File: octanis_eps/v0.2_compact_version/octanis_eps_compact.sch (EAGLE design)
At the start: 152 parts, among them IC10 OPA2333DGK, IC11 OPA2333DGK, IC12 OPA2333DGK, IC2 OPA2333DGK, IC3 OPA2333DGK, IC4 OPA2333DGK, IC5 OPA2333DGK, IC6 OPA2333DGK, IC7 OPA2333DGK, IC8 OPA2333DGK, IC9 OPA2333DGK, Q1 FC-12M

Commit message: modified compact version schematics
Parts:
- removed C1: 10nF, rcl:C-EUC0603
- removed C12: 1uF, rcl:CPOL-EUA/3216-18R
- removed C13: 470pF, rcl:C-EUC0603
- removed C16: 1n, rcl:C-EUC0603
- removed C17: 1u, rcl:CPOL-EUA/3216-18R
- removed C18: 1u, rcl:C-EUC0603
- removed C19: 22u, rcl:CPOL-EUA/3216-18R
- removed C_IC10, C_IC11, C_IC12, C_IC2, C_IC4, C_IC8: 100nF, rcl:C-EUC0603
- removed DISSIP1, DISSIP2: MP725TO-252, Octanis1_EPS:MP725TO-252
- removed IC10, IC11, IC12, IC2, IC4, IC8: OPA2333DGK, linear:OPA2333DGK
- removed L1: 4.7uH, inductors:DR73
- removed L2: 0.47uH, inductors:DR73
- removed LTC3411: LT3411, Octanis1_EPS:LT3411
- removed R30, R31, R4: 162k, rcl:R-EU_R0603
- removed R33, R38, R46, R47, R49, R50, R65: 100k, rcl:R-EU_R0603
- removed R34: 13k7, rcl:R-EU_R0603
- removed R35: 29k4, rcl:R-EU_R0603
- removed R36, R44: 19k6, rcl:R-EU_R0603
- removed R37: 27k4, rcl:R-EU_R0603
- removed R39, R57: 50m, rcl:R-EU_R1206
- removed R40, R41, R63, R71: 22k1, rcl:R-EU_R0603
- removed R42, R5: 75k, rcl:R-EU_R0603
- removed R43, R45, R58, R62: 270k, rcl:R-EU_R0603
- removed R51, R52, R53: 200k, rcl:R-EU_R0603
- removed R54, R61, R64, R70: 1M, rcl:R-EU_R0603
- removed R55: 140k, rcl:R-EU_R0603
- removed R56: 43k2, rcl:R-EU_R0603
- removed R59: 330k, rcl:R-EU_R0603
- removed R60: 24k9, rcl:R-EU_R0603
- removed SC_BOT: (no value), jumper:JP4E
- added 0.47UH, 10UH: DR127, inductors:DR127
- added HEAT1, HEAT2, HEAT3, HEAT_SINK: (no value), jumper:JP1E
- added U$10, U$9: MBRM120LTIG, Octanis1_EPS:MBRM120LTIG
- added U$12, U$20, U$21: IRFR3711ZTRPBF, Octanis1_EPS:IRFR3711ZTRPBF
- C10: value 100nF -> 22u
- C11: value 100nF -> 4.7p
- C4: value 150nF -> 4.7u
- C5: value 150nF -> 470p
- C8: value 1nF -> 22u
- C9: value 22uF -> 10u; device rcl:CPOL-EUA/3216-18R -> rcl:C-EUC0603
- R1: value 33k -> 1k
- R10: value 50m -> 30.1k; device rcl:R-EU_R1206 -> rcl:R-EU_R0603
- R11: value 10k -> 549k
- R12: value 50m -> 1.3M; device rcl:R-EU_R1206 -> rcl:R-EU_R0603
- R13: value 10k -> 1M
- R2: value 20k -> 1k
- R3: value 1M -> 1k
- R32: value 162k -> 82k
- U$11: value LTC3421 -> MBRM120LTIG; device Octanis1_EPS:LTC3421 -> Octanis1_EPS:MBRM120LTIG
- U$2, U$3: value MAX4376FASASO8 -> INA213; device Octanis1_EPS:MAX4376FASASO8 -> Octanis1_EPS:INA213
- U$4: value MAX4376FASASO8 -> LTC3402; device Octanis1_EPS:MAX4376FASASO8 -> Octanis1_EPS:LTC3402
- U$5: value MAX4376FASASO8 -> TPS62086; device Octanis1_EPS:MAX4376FASASO8 -> Octanis1_EPS:TPS62086
- U$8: value FDV301N -> MBRM120LTIG; device Octanis1_EPS:FDV301N -> Octanis1_EPS:MBRM120LTIG
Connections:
- removed net BT_IN: BT_IN.3, BT_IN.4, R10.1, R12.2, U$4.RS+, U$5.RS-
- removed net CHG_CMD: C1.2, IC2B.OUT, R31.2, R49.2
- removed net I_CHG_MS: IC4A.-IN, IC4A.OUT, U$1.7
- removed net I_DSG_MS: IC4B.-IN, IC4B.OUT, U$1.8
- removed net N$32: R37.1, U$11.RT
- removed net N$33: C11.2, U$11.SS
- removed net N$35: C18.2, R60.2
- removed net N$36: R38.1, U$11.VC
- removed net N$38: IC10B.+IN, R40.2, R45.2
- removed net N$39: IC10B.-IN, R41.2, R43.1
- removed net N$40: R9.2, U$2.OUT
- removed net N$41: R11.2, U$4.OUT
- removed net N$42: R7.2, U$3.OUT
- removed net N$43: R13.2, U$5.OUT
- removed net N$44: IC8A.OUT, U$6.B
- removed net N$46: DISSIP2.B, IC9A.-IN, U$7.E
- removed net N$47: DISSIP1.B, IC8A.-IN, U$6.E
- removed net N$5: C4.2, IC4A.+IN, R11.1
- removed net N$51: C16.1, IC11B.OUT, R54.2
- removed net N$52: IC11A.-IN, R49.1, R50.2
- removed net N$53: IC11A.OUT, R50.1, R51.2
- removed net N$54: IC11B.-IN, R51.1, R52.2, R53.2
- removed net N$55: C16.2, R52.1
- removed net N$56: IC12A.OUT, R53.1, R58.2
- removed net N$57: LTC3411.VFB, R54.1, R55.2, R56.1
- removed net N$58: C17.+, L2.2, R55.1, R57.2, R71.1
- removed net N$59: LTC3411.ITH, R60.1
- removed net N$60: LTC3411.SYNC/MODE, R61.2, R64.1
- removed net N$61: IC12A.-IN, R58.1, R71.2
- removed net N$62: LTC3411.SHDN/RT, R59.1
- removed net N$63: IC12A.+IN, R62.2, R63.2
- removed net N$64: LTC3411.PGOOD, R65.2
- removed net N$65: R59.2, R70.2, U$8.D
- removed net N$75: C9.+, R35.1, R36.1, R39.2, R41.1, U$11.VOUT1, U$11.VOUT2, U$11.VOUT3, U$11.VOUTS
- removed net N$77: L2.1, LTC3411.SW
- removed net N$78: L1.2, U$11.SW1, U$11.SW2, U$11.SW3
- removed net UUU: IC10B.OUT, R30.2, R43.2
- new net DISSIP: HEAT_SINK.2, U$11.K, U$12.D, U$20.D, U$21.D, U$8.K, U$9.K
- new net DISSIP1: IC9A.-IN, U$11.A, U$7.E
- new net DISSIP2: IC9B.-IN, U$6.E, U$9.A
- new net EN_HEAT1: R1.2, U$1.34
- new net EN_HEAT2: R2.2, U$1.35
- new net EN_HEAT3: R3.2, U$1.36
- new net HEAT1: HEAT1.2, U$12.S
- new net HEAT2: HEAT2.2, U$21.S
- new net HEAT3: HEAT3.2, U$20.S
- net +3V3: no longer R46.1, R47.1
- net BT+: now also BT_IN.3, BT_IN.4, C8.2, C9.2, U$10.K, U$4.VOUT, U$5.EN, U$5.VIN; no longer C19.+, LTC3411.PVIN, LTC3411.SVIN, R10.2, R39.1, R40.1, R61.1, R65.1, R70.1, U$4.RS-, U$5.RS+
- net EN_CHG: now also U$4.SHDN; no longer IC9B.+IN, U$8.G
- net EXT_PW: now also U$2.IN-; no longer U$3.RS-
- net GND: now also C8.1, C9.1, HEAT1.1, HEAT2.1, HEAT3.1, HEAT_SINK.1, R10.2, R11.1, R32.2, U$2.REF, U$3.REF, U$4.MODE; no longer C12.-, C13.1, C17.-, C18.1, C19.-, C5.1, C9.-, C_IC10.1, C_IC11.1, C_IC12.1, C_IC2.1, C_IC4.1, C_IC8.1, DISSIP1.A, DISSIP1.NC, DISSIP2.A, DISSIP2.NC, IC10P.V-, IC11P.V-, IC12P.V-, IC2P.V-, IC4P.V-, IC8B.+IN, IC8B.-IN, IC8P.V-, LTC3411.PGND, LTC3411.SGND, R2.1, R34.2, R37.2, R42.2, R44.2, R56.2, R64.2, SC_BOT.3, SC_BOT.4, U$11.ENB, U$11.EP, U$11.GND, U$11.LB1, U$11.PGND1, U$11.PGND2, U$11.PGND3, U$11.SYNC, U$8.S
- net I2C_SCL: no longer R46.2
- net I2C_SDA: no longer R47.2
- net N$1: now also R7.2, U$2.OUT; no longer IC2A.-IN, R1.1, R2.2, R3.2
- net N$2: now also R9.2, U$3.OUT; no longer IC2A.OUT, R3.1, R5.2
- net N$22: now also IC9B.+IN; no longer IC8A.+IN
- net N$23: now also R11.2, R12.2, U$4.FB; no longer IC10A.-IN, R30.1, R31.1, R32.2
- net N$24: now also 10UH.2, U$10.A, U$4.SW; no longer C8.2, R32.1
- net N$25: now also R13.2, U$5.PG; no longer C8.1, IC10A.OUT, R33.2
- net N$26: now also 0.47UH.1, U$5.SW; no longer R33.1, R34.1, R35.2, U$11.FB
- net N$29: now also R1.1, U$12.G; no longer R42.1, U$11.ILIM
- net N$3: now also R10.1, U$4.RT; no longer C1.1, R4.1
- net N$30: now also IC9B.OUT, U$6.B; no longer C10.2, R36.2, R44.1, U$11.BURST
- net N$31: now also R2.1, U$21.G; no longer C13.2, R38.2
- net N$37: now also R3.1, U$20.G; no longer IC9B.-IN, IC9B.OUT, U$11.SHDN
- net N$4: now also C5.1, R32.1; no longer IC2B.-IN, R4.2, R5.1
- net N$8: now also C11.2, U$4.VC; no longer IC4B.+IN, R13.1
- net SC+: now also U$3.IN+; no longer SC_BOT.1, SC_BOT.2, U$2.RS+
- net VCC: now also 0.47UH.2, 10UH.1, C10.2, C4.2, R13.1, U$2.IN+, U$3.IN-, U$4.VIN, U$5.FB, U$5.VOS, U$8.A; no longer C12.+, C_IC10.2, C_IC11.2, C_IC12.2, C_IC2.2, C_IC4.2, C_IC8.2, IC10P.V+, IC11P.V+, IC12P.V+, IC2P.V+, IC4P.V+, IC8P.V+, L1.1, R1.2, R57.1, R63.1, U$11.VIN, U$2.RS-, U$3.RS+, U$4.VCC, U$5.VCC
- net VREF: no longer IC10A.+IN, IC11A.+IN, IC11B.+IN, IC2A.+IN, IC2B.+IN, R45.1, R62.1
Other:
- note added: "DISSIPATION"
- note added: "Dissipation control"
- note removed: "BT_CHG"
- note removed: "BT_DSG"
- note removed: "Bus regulation"
- note removed: "Solar Bot input"
- moved on the sheet: C10, C11, C2, C3, C4, C5, C8, IC3A, IC3B, IC9A, IC9B, R1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

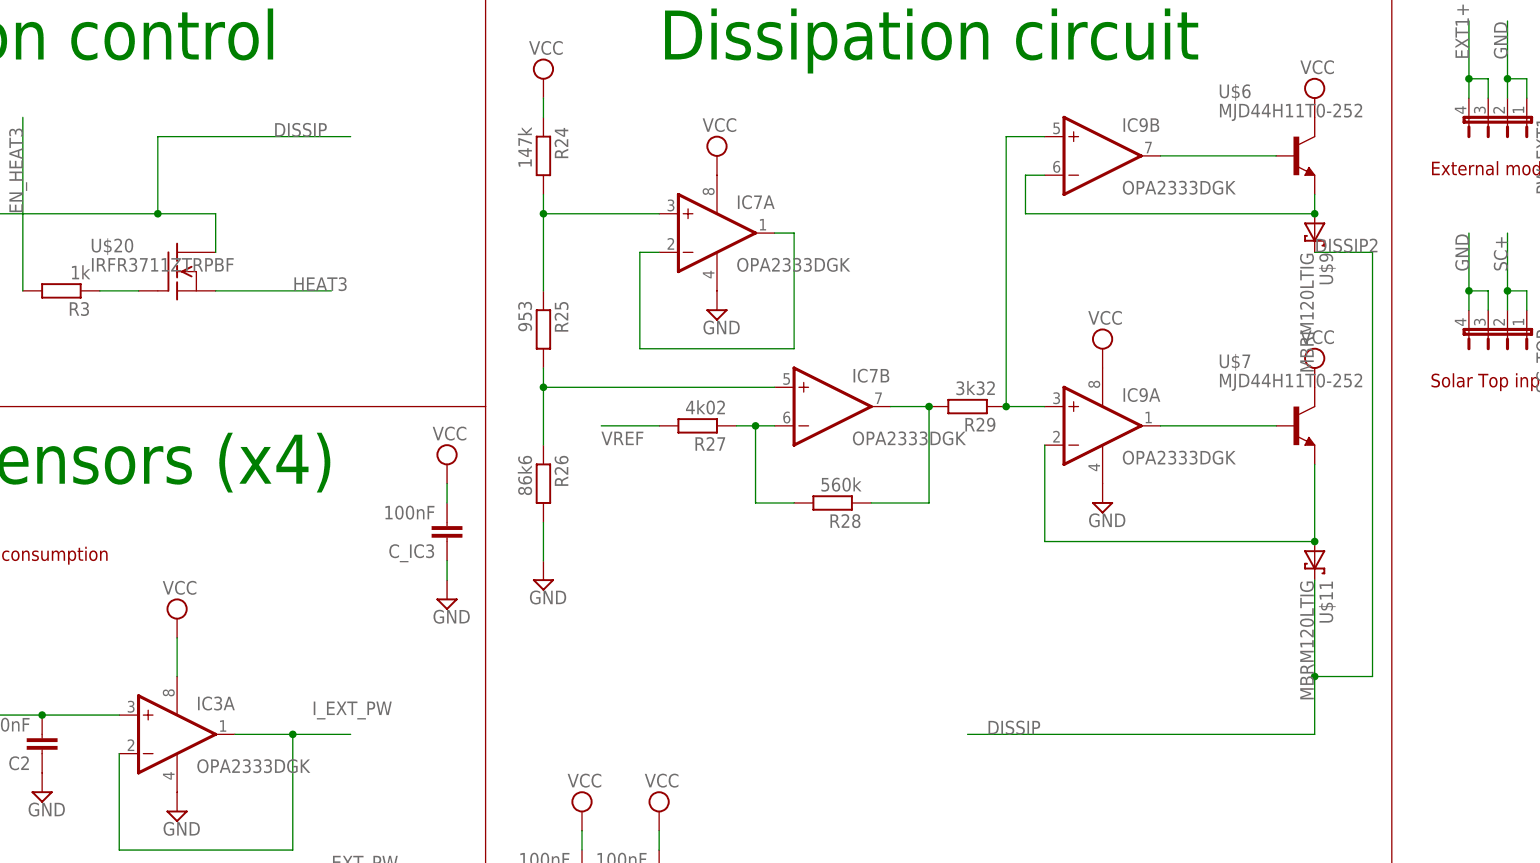
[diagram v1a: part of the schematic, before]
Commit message: corrected zener connection error
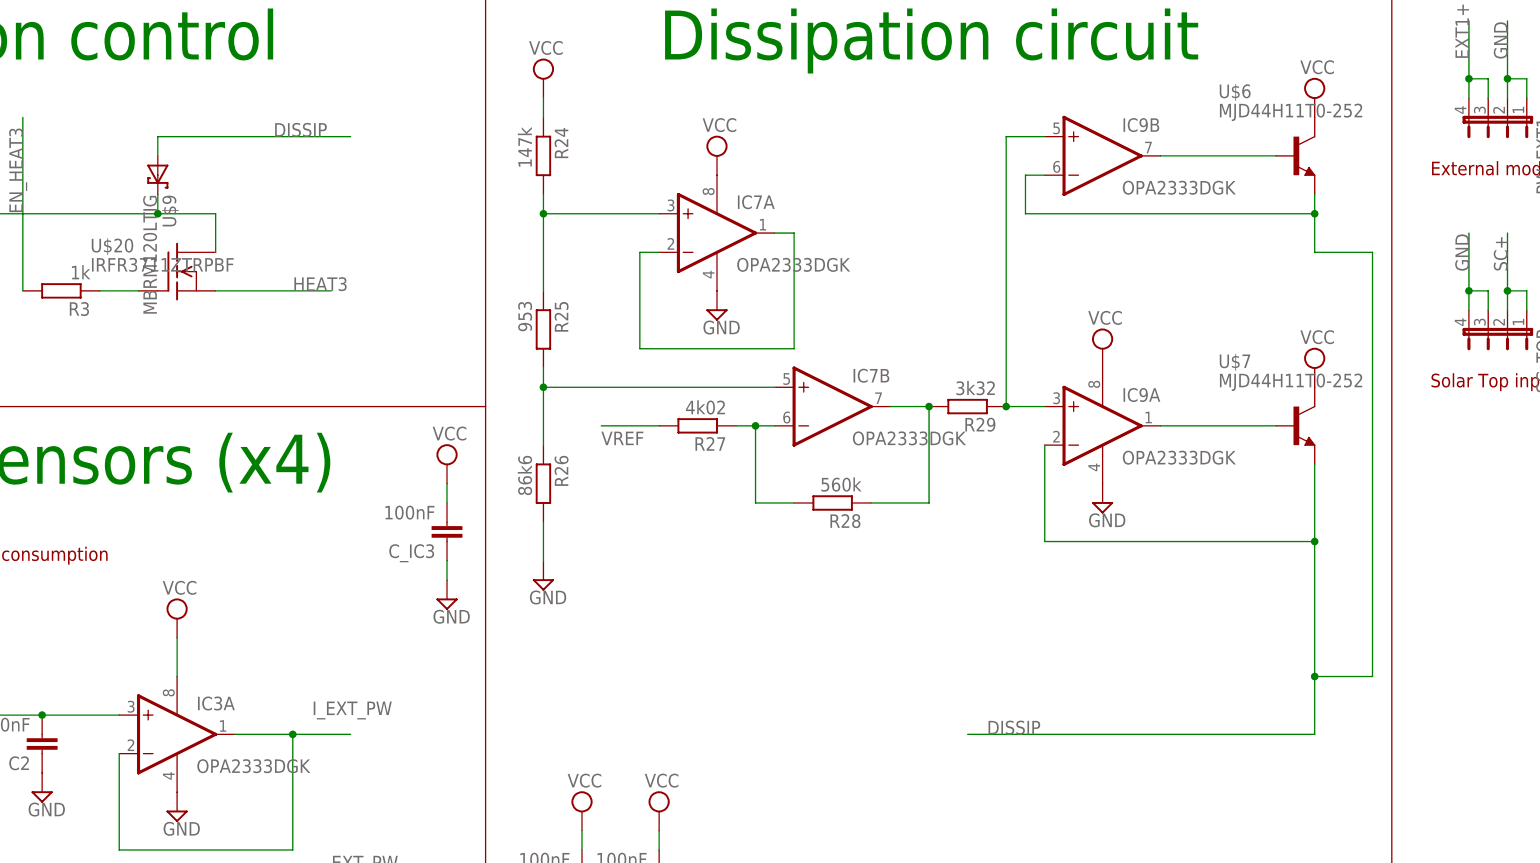
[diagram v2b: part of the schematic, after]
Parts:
- removed U$11: MBRM120LTIG, Octanis1_EPS:MBRM120LTIG
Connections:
- removed net DISSIP1: IC9A.-IN, U$11.A, U$7.E
- removed net DISSIP2: IC9B.-IN, U$6.E, U$9.A
- net DISSIP: now also IC9A.-IN, IC9B.-IN, U$6.E, U$7.E, U$9.A; no longer U$11.K
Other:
- moved on the sheet: U$9
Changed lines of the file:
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@@
 <part name="U$20" library="Octanis1_EPS" deviceset="IRFR3711ZTRPBF" device=""/>
 <part name="U$21" library="Octanis1_EPS" deviceset="IRFR3711ZTRPBF" device=""/>
-<part name="U$9" library="Octanis1_EPS" deviceset="MBRM120LTIG" device=""/>
-<part name="U$11" library="Octanis1_EPS" deviceset="MBRM120LTIG" device=""/>
 <part name="HEAT1" library="jumper" deviceset="JP1E" device=""/>
 <part name="HEAT2" library="jumper" deviceset="JP1E" device=""/>
@@
 <part name="HEAT_SINK" library="jumper" deviceset="JP1E" device=""/>
 <part name="SUPPLY50" library="supply2" deviceset="GND" device=""/>
+<part name="U$9" library="Octanis1_EPS" deviceset="MBRM120LTIG" device=""/>
 </parts>
 <sheets>
@@
 <instance part="U$20" gate="G$1" x="53.34" y="63.5"/>
 <instance part="U$21" gate="G$1" x="-2.54" y="53.34"/>
-<instance part="U$9" gate="G$1" x="203.2" y="68.58" rot="R270"/>
-<instance part="U$11" gate="G$1" x="203.2" y="25.4" rot="R270"/>
 <instance part="HEAT1" gate="A" x="391.16" y="71.12" rot="R180"/>
 <instance part="HEAT2" gate="A" x="401.32" y="71.12" rot="R180"/>
@@
 <instance part="HEAT_SINK" gate="A" x="421.64" y="71.12" rot="R180"/>
 <instance part="SUPPLY50" gate="GND" x="406.4" y="78.74" rot="R180"/>
+<instance part="U$9" gate="G$1" x="50.8" y="76.2" rot="R270"/>
 </instances>
 <busses>
@@
 </segment>
 </net>
-<net name="DISSIP1" class="0">
-<segment>
-<pinref part="IC9" gate="A" pin="-IN"/>
-<wire x1="167.64" y1="27.94" x2="167.64" y2="40.64" width="0.1524" layer="91"/>
-<pinref part="U$7" gate="G$1" pin="E"/>
-<wire x1="203.2" y1="38.1" x2="203.2" y2="27.94" width="0.1524" layer="91"/>
-<wire x1="167.64" y1="27.94" x2="203.2" y2="27.94" width="0.1524" layer="91"/>
-<pinref part="U$11" gate="G$1" pin="A"/>
-<junction x="203.2" y="27.94"/>
-</segment>
-</net>
-<net name="DISSIP2" class="0">
-<segment>
-<wire x1="165.1" y1="76.2" x2="165.1" y2="71.12" width="0.1524" layer="91"/>
-<wire x1="165.1" y1="71.12" x2="203.2" y2="71.12" width="0.1524" layer="91"/>
-<pinref part="U$6" gate="G$1" pin="E"/>
-<wire x1="203.2" y1="71.12" x2="203.2" y2="73.66" width="0.1524" layer="91"/>
-<pinref part="IC9" gate="B" pin="-IN"/>
-<wire x1="165.1" y1="76.2" x2="167.64" y2="76.2" width="0.1524" layer="91"/>
-<label x="203.2" y="66.04" size="1.778" layer="95"/>
-<pinref part="U$9" gate="G$1" pin="A"/>
-<junction x="203.2" y="71.12"/>
-</segment>
-</net>
 <net name="N$30" class="0">
 <segment>
@@
 </net>
 <net name="DISSIP" class="0">
-<segment>
-<pinref part="U$11" gate="G$1" pin="K"/>
-<wire x1="203.2" y1="22.86" x2="203.2" y2="10.16" width="0.1524" layer="91"/>
-<pinref part="U$9" gate="G$1" pin="K"/>
-<wire x1="203.2" y1="10.16" x2="203.2" y2="2.54" width="0.1524" layer="91"/>
-<wire x1="203.2" y1="66.04" x2="210.82" y2="66.04" width="0.1524" layer="91"/>
-<wire x1="210.82" y1="66.04" x2="210.82" y2="10.16" width="0.1524" layer="91"/>
-<wire x1="210.82" y1="10.16" x2="203.2" y2="10.16" width="0.1524" layer="91"/>
-<junction x="203.2" y="10.16"/>
-<wire x1="203.2" y1="2.54" x2="157.48" y2="2.54" width="0.1524" layer="91"/>
-<label x="160.02" y="2.54" size="1.778" layer="95"/>
-</segment>
 <segment>
 <pinref part="U$8" gate="G$1" pin="K"/>
@@
 <wire x1="7.62" y1="71.12" x2="2.54" y2="71.12" width="0.1524" layer="91"/>
 <junction x="7.62" y="71.12"/>
-<wire x1="50.8" y1="71.12" x2="50.8" y2="81.28" width="0.1524" layer="91"/>
+<pinref part="U$9" gate="G$1" pin="K"/>
+<wire x1="50.8" y1="73.66" x2="50.8" y2="71.12" width="0.1524" layer="91"/>
 <junction x="50.8" y="71.12"/>
-<wire x1="50.8" y1="81.28" x2="76.2" y2="81.28" width="0.1524" layer="91"/>
-<label x="66.04" y="81.28" size="1.778" layer="95"/>
 </segment>
 <segment>
@@
 <label x="419.1" y="58.42" size="1.778" layer="95" rot="R90"/>
 </segment>
-</net>
+<segment>
+<wire x1="165.1" y1="76.2" x2="165.1" y2="71.12" width="0.1524" layer="91"/>
+<wire x1="165.1" y1="71.12" x2="203.2" y2="71.12" width="0.1524" layer="91"/>
+<pinref part="U$6" gate="G$1" pin="E"/>
+<wire x1="203.2" y1="71.12" x2="203.2" y2="73.66" width="0.1524" layer="91"/>
+<pinref part="IC9" gate="B" pin="-IN"/>
+<wire x1="165.1" y1="76.2" x2="167.64" y2="76.2" width="0.1524" layer="91"/>
+<wire x1="203.2" y1="27.94" x2="203.2" y2="10.16" width="0.1524" layer="91"/>
+<wire x1="203.2" y1="10.16" x2="203.2" y2="2.54" width="0.1524" layer="91"/>
+<wire x1="203.2" y1="66.04" x2="210.82" y2="66.04" width="0.1524" layer="91"/>
+<wire x1="210.82" y1="66.04" x2="210.82" y2="10.16" width="0.1524" layer="91"/>
+<wire x1="210.82" y1="10.16" x2="203.2" y2="10.16" width="0.1524" layer="91"/>
+<junction x="203.2" y="10.16"/>
+<wire x1="203.2" y1="2.54" x2="157.48" y2="2.54" width="0.1524" layer="91"/>
+<label x="160.02" y="2.54" size="1.778" layer="95"/>
+<wire x1="203.2" y1="71.12" x2="203.2" y2="66.04" width="0.1524" layer="91"/>
+<junction x="203.2" y="71.12"/>
+<pinref part="IC9" gate="A" pin="-IN"/>
+<wire x1="167.64" y1="27.94" x2="167.64" y2="40.64" width="0.1524" layer="91"/>
+<pinref part="U$7" gate="G$1" pin="E"/>
+<wire x1="203.2" y1="38.1" x2="203.2" y2="27.94" width="0.1524" layer="91"/>
+<wire x1="167.64" y1="27.94" x2="203.2" y2="27.94" width="0.1524" layer="91"/>
+<junction x="203.2" y="27.94"/>
+</segment>
+<segment>
+<wire x1="50.8" y1="81.28" x2="76.2" y2="81.28" width="0.1524" layer="91"/>
+<label x="66.04" y="81.28" size="1.778" layer="95"/>
+<pinref part="U$9" gate="G$1" pin="A"/>
+<wire x1="50.8" y1="81.28" x2="50.8" y2="78.74" width="0.1524" layer="91"/>
+</segment>
+</net>
